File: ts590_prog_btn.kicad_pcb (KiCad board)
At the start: 2 copper layers, 18 parts, among them J1 DB9, SW1 PTT, SW2 PF2, SW3 PF4, SW4 PF1, SW5 PF3, SW6 UP, SW7 DOWN, SW8 MIC_EXT_PWR, SW9 PTT_LOCK

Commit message: added the first pcb draw
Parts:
- added REF**: EuroBoard_viertel_Type-I_80mmX50mm_holes, EuroBoard_Outline:EuroBoard_viertel_Type-I_80mmX50mm_holes, F.Cu at (109.5, 99.3)
- added REF**: Symbol_CreativeCommons_CopperTop_Type2_Small, Symbols:Symbol_CreativeCommons_CopperTop_Type2_Small, F.Cu at (176.5, 94.6)
- added REF**: Symbol_CreativeCommonsPublicDomain_CopperTop_Small, Symbols:Symbol_CreativeCommonsPublicDomain_CopperTop_Small, F.Cu at (149.2, 53.3)
- moved J1 95.2 mm to (173.7, 74.2), turned to 270 degrees
- moved SW9 60.7 mm to (125.0, 76.7), turned to 270 degrees
- moved SW8 59.8 mm to (161.8, 84.1), turned to 180 degrees
- moved SW3 52.8 mm to (163.1, 70.1)
- moved R2 49.5 mm to (164.3, 76.2)
- moved R6 46.3 mm to (149.4, 87.9), turned to 180 degrees
- moved SW7 40.1 mm to (152.9, 61.5)
- moved C1 39.2 mm to (164.3, 62.0)
- moved SW5 33.5 mm to (152.9, 70.1)
- moved R4 32.2 mm to (149.1, 76.2)
- moved R3 31.5 mm to (125.5, 61.5), turned to 90 degrees
- moved R5 31.2 mm to (149.4, 84.3)
- moved C2 26.7 mm to (138.2, 84.3), turned to 90 degrees
- moved SW6 22.9 mm to (142.7, 61.5)
- moved R1 22.7 mm to (121.9, 61.5), turned to 90 degrees
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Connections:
- J1 pad 6: Net-(J1-Pad6) -> (no net)
- J1 pad 9: Net-(J1-Pad9) -> (no net)
- SW8 pad 2: /EXTMIC -> (no net)
- SW8 pad 6: Net-(SW8-Pad6) -> (no net)
- SW9 pad 1: Net-(SW9-Pad1) -> (no net)
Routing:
- net /MICCN4_UP: track 0.00 -> 111.3 mm
- net /MICCN2_PTT: track 0.00 -> 80.3 mm
- net GNDA: track 0.00 -> 51.3 mm
- net /MICCN3_DOWN: track 0.00 -> 44.8 mm
- net /MIC_ELECT: track 0.00 -> 39.4 mm
- net Net-(R1-Pad1): track 0.00 -> 29.3 mm
- net /MICCN1_MIC: track 0.00 -> 27.6 mm
- net Net-(R3-Pad1): track 0.00 -> 15.1 mm
- net /MICCN5_8V: track 0.00 -> 14.2 mm
- net Net-(R4-Pad1): track 0.00 -> 14.2 mm
- net Net-(R2-Pad1): track 0.00 -> 11.2 mm
- net GND: track 0.00 -> 9.71 mm, vias 0 -> 1
- net Net-(C2-Pad1): track 0.00 -> 9.65 mm
- net /MICCN5_8V_PWRSW: track 0.00 -> 4.83 mm
- added copper zone on F.Cu, net GND
- added copper zone on B.Cu, net GNDA
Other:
- board outline added: 80 x 50 mm
- net class Default: trace_width 0.25 -> 0.254; via_dia 0.6 -> 1; via_drill 0.4 -> 0.5
- net class PWR added: clearance 0.2, trace_width 0.6, via_dia 1, via_drill 0.5
- board text added: "CT7AEZ"
- board text added: "Este trabalho está licenciado sob uma Licença Creative Commons Atribuição 4.0 Internacional. Para ver uma cópia desta licença, visite http://creativecommons.org/licenses/by/4.0/."

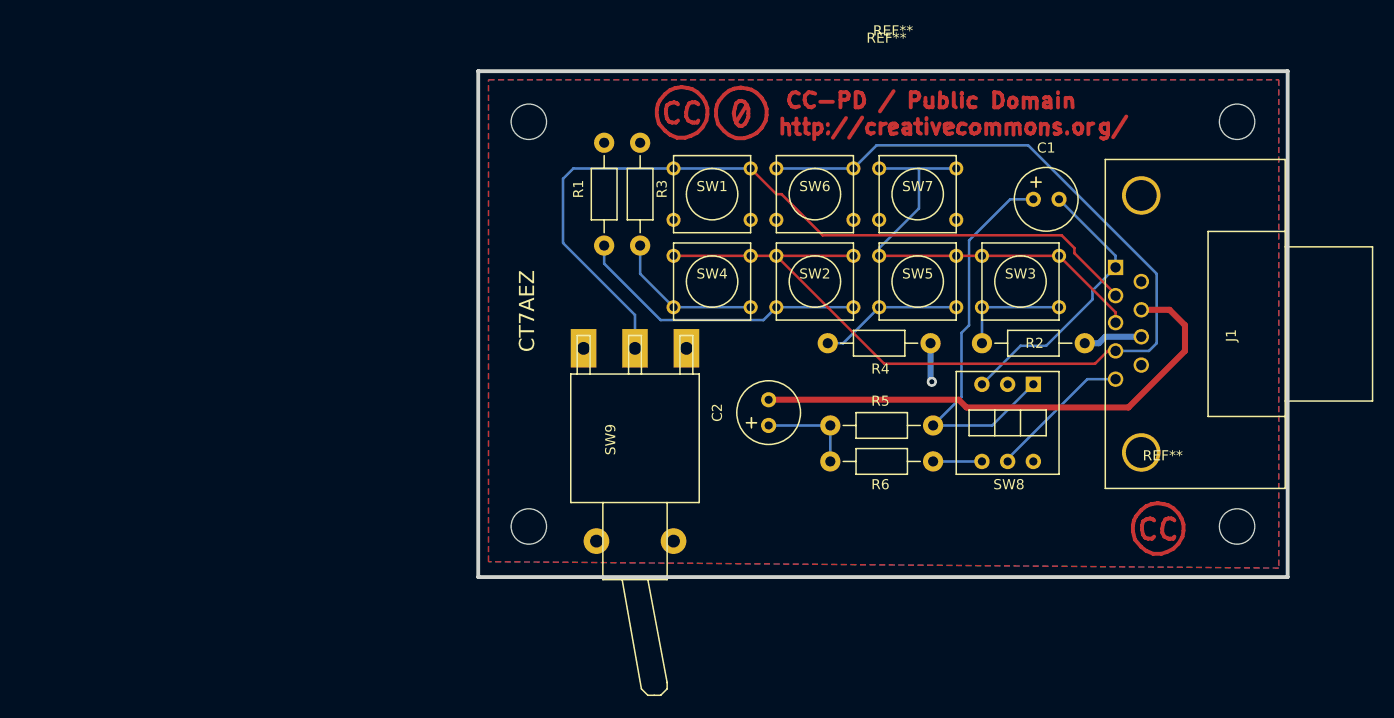
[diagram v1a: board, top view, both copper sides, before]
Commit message: add jack on pcb and new layout
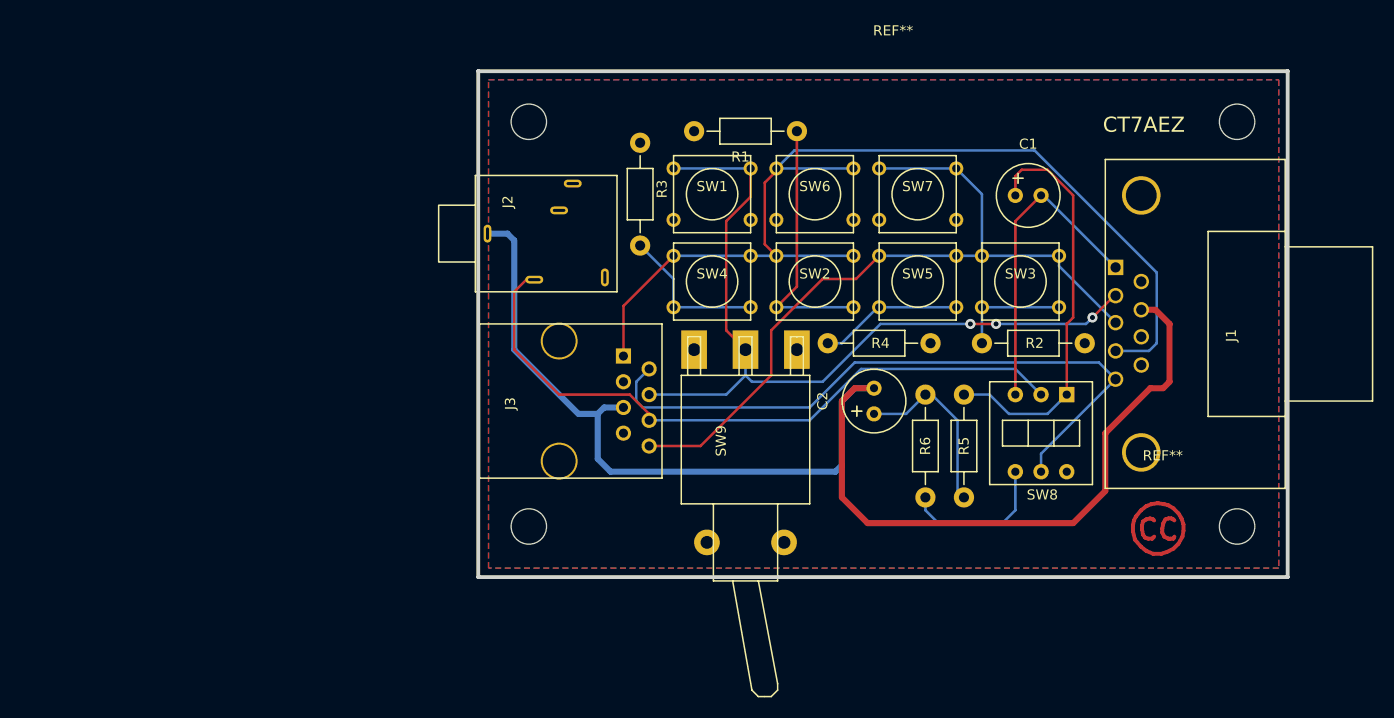
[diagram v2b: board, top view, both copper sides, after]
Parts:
- removed the REF** at (149.2, 53.3)
- added J2: JACK_TRS_6PINS, TS-590-Program-Function-extention:myaudiojack, F.Cu at (123.2, 71.1)
- added J3: RJ45, Connect:RJ45_8, F.Cu at (117.5, 81.9)
- moved R1 15.3 mm to (135.9, 55.2), turned to 180 degrees
- moved SW9 10.9 mm to (135.9, 76.8)
- moved C2 10.5 mm to (148.6, 83.2)
- moved R5 8.38 mm to (157.5, 86.4), turned to 90 degrees
- moved R6 4.58 mm to (153.7, 86.4), turned to 90 degrees
- moved SW8 3.45 mm to (165.1, 85.1)
- moved C1 1.82 mm to (162.6, 61.6)
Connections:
- SW8 pad 2: (no net) -> /EXTMIC
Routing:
- net GNDA: track 51.3 -> 131.7 mm
- net /EXTMIC: track 0.00 -> 67.3 mm
- net /MICCN5_8V: track 14.2 -> 66.1 mm
- net /MICCN3_DOWN: track 44.8 -> 77.1 mm
- net /MICCN5_8V_PWRSW: track 4.83 -> 15.0 mm
- net GND: track 9.71 -> 0.00 mm, vias 1 -> 0
- net /MICCN4_UP: track 111.3 -> 101.6 mm
- net Net-(C2-Pad1): track 9.65 -> 18.0 mm
- net /MICCN1_MIC: track 27.6 -> 31.0 mm
- net Net-(R1-Pad1): track 29.3 -> 26.5 mm
- net /MIC_ELECT: track 39.4 -> 40.6 mm
- net /MICCN2_PTT: track 80.3 -> 80.5 mm, vias 0 -> 3
- added copper zone on B.Cu, net GND
- removed copper zone on B.Cu, net GNDA
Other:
- board text removed: "Este trabalho está licenciado sob uma Licença Creative Commons Atribuição 4.0 Internacional. Para ver uma cópia desta licença, visite http://creativecommons.org/licenses/by/4.0/."

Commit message: Corrected the mic pwr selection on pcb and sch.
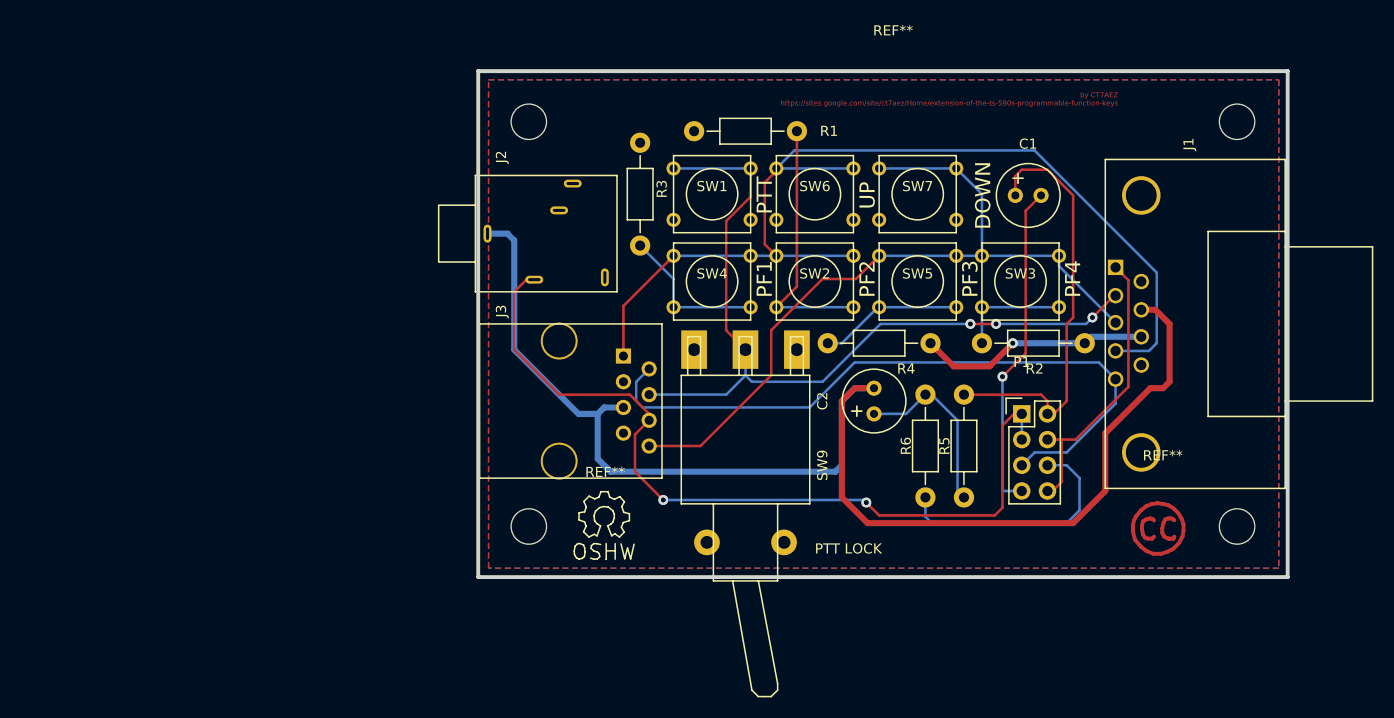
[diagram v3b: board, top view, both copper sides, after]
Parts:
- removed SW8: MIC_EXT_PWR, Discret:swdip3
- added P1: CONN_02X04, Pin_Headers:Pin_Header_Straight_2x04, F.Cu at (163.2, 83.2)
- added REF**: Symbol_OSHW-Logo_SilkScreen, Symbols:Symbol_OSHW-Logo_SilkScreen, F.Cu at (121.9, 93.3)
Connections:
- C1 pad 2: /MICCN1_MIC -> Net-(C1-Pad2)
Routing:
- net Net-(C1-Pad2): track 0.00 -> 32.9 mm, vias 0 -> 1
- net GND: track 0.00 -> 23.0 mm, vias 0 -> 1
- net /EXTMIC: track 67.3 -> 82.6 mm, vias 0 -> 2
- net /MICCN5_8V_PWRSW: track 15.0 -> 24.8 mm
- net /MICCN1_MIC: track 31.0 -> 28.5 mm
- net /MICCN5_8V: track 66.1 -> 68.1 mm
- net /MIC_ELECT: track 40.6 -> 41.7 mm
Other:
- board text added: "DOWN"
- board text added: "MIC PWR"
- board text added: "NO MIC PWR"
- board text added: "PF1"
- board text added: "PF2"
- board text added: "PF3"
- board text added: "PF4"
- board text added: "PTT"
- board text added: "PTT LOCK"
- board text added: "UP"
- board text added: "by CT7AEZ https://sites.google.com/site/ct7aez/Home/extension-of-the-ts-590s-programmable-function-keys"
- board text removed: "CT7AEZ"

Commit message: small changes on pcb
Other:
- rule pad_to_mask_clearance: 0 -> 0.2
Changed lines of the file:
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@@
     (pad_size 1.5 1.5)
     (pad_drill 0.6)
-    (pad_to_mask_clearance 0)
+    (pad_to_mask_clearance 0.2)
     (aux_axis_origin 0 0)
     (visible_elements FFFFFF7F)
     (pcbplotparams
-      (layerselection 0x00030_80000001)
-      (usegerberextensions false)
+      (layerselection 0x030f0_80000001)
+      (usegerberextensions true)
       (excludeedgelayer true)
       (linewidth 0.100000)
@@
       (outputformat 1)
       (mirror false)
-      (drillshape 1)
+      (drillshape 0)
       (scaleselection 1)
-      (outputdirectory ""))
+      (outputdirectory gerb/))
   )
   (net 0 "")
@@
     (add_net GNDA)
   )
+  (module Capacitors_Elko_ThroughHole:Elko_vert_11.2x6.3mm_RM2.5 (layer F.Cu)
+    (at 148.59 83.185 90)
+    (descr "Electrolytic Capacitor, vertical, diameter 6,3mm, RM 2,5mm, radial,")
+    (tags "Electrolytic Capacitor, vertical, diameter 6,3mm, RM 2,5mm, Elko, Electrolytkondensator, Kondensator gepolt, Durchmesser 6,3mm, radial,")
+    (fp_text reference C2 (at 1.27 -5.08 90) (layer F.SilkS)
+      (effects (font (size 1 1) (thickness 0.15)))
+    )
+    (fp_text value 10u (at 1.27 5.08 90) (layer F.Fab)
+      (effects (font (size 1 1) (thickness 0.15)))
+    )
+    (fp_line (start 0.26924 -2.19964) (end 0.26924 -1.19888) (layer F.SilkS) (width 0.15))
+    (fp_line (start -0.23114 -1.69926) (end 0.76962 -1.69926) (layer F.SilkS) (width 0.15))
+    (fp_circle (center 1.27 0) (end 4.4196 0) (layer F.SilkS) (width 0.15))
+    (pad 2 thru_hole circle (at 2.54 0 90) (size 1.50114 1.50114) (drill 0.8001) (layers *.Cu *.Mask F.SilkS)
+      (net 3 GNDA))
+    (pad 1 thru_hole circle (at 0 0 90) (size 1.50114 1.50114) (drill 0.8001) (layers *.Cu *.Mask F.SilkS)
+      (net 4 "Net-(C2-Pad1)"))
+    (model Capacitors_Elko_ThroughHole.3dshapes/Elko_vert_11.2x6.3mm_RM2.5.wrl
+      (at (xyz 0 0 0))
+      (scale (xyz 1 1 1))
+      (rotate (xyz 0 0 0))
+    )
+  )
   (module EuroBoard_Outline:EuroBoard_viertel_Type-I_80mmX50mm_holes (layer F.Cu)
     (at 109.474 99.314)
     (descr "Outline, Eurocard 1/4, Type I,  80x50mm, with holes 3,5mm,")
     (tags "Outline, Eurocard 1/4, Type I, 80x50mm, with holes 3,5mm,")
-    (fp_text reference REF** (at 41.00068 -54.0004) (layer F.SilkS)
+    (fp_text reference REF** (at 41.00068 -54.0004) (layer F.SilkS) hide
       (effects (font (size 1 1) (thickness 0.15)))
     )
@@
     (pad 1 thru_hole circle (at 0 0) (size 1.50114 1.50114) (drill 0.8001) (layers *.Cu *.Mask F.SilkS)
       (net 2 /MIC_ELECT))
-    (model Capacitors_Elko_ThroughHole.3dshapes/Elko_vert_11.2x6.3mm_RM2.5.wrl
-      (at (xyz 0 0 0))
-      (scale (xyz 1 1 1))
-      (rotate (xyz 0 0 0))
-    )
-  )
-  (module Capacitors_Elko_ThroughHole:Elko_vert_11.2x6.3mm_RM2.5 (layer F.Cu)
-    (at 148.59 83.185 90)
-    (descr "Electrolytic Capacitor, vertical, diameter 6,3mm, RM 2,5mm, radial,")
-    (tags "Electrolytic Capacitor, vertical, diameter 6,3mm, RM 2,5mm, Elko, Electrolytkondensator, Kondensator gepolt, Durchmesser 6,3mm, radial,")
-    (fp_text reference C2 (at 1.27 -5.08 90) (layer F.SilkS)
-      (effects (font (size 1 1) (thickness 0.15)))
-    )
-    (fp_text value 10u (at 1.27 5.08 90) (layer F.Fab)
-      (effects (font (size 1 1) (thickness 0.15)))
-    )
-    (fp_line (start 0.26924 -2.19964) (end 0.26924 -1.19888) (layer F.SilkS) (width 0.15))
-    (fp_line (start -0.23114 -1.69926) (end 0.76962 -1.69926) (layer F.SilkS) (width 0.15))
-    (fp_line (start 0.26924 -1.69926) (end 0.76962 -1.69926) (layer F.Cu) (width 0.15))
-    (fp_line (start 0.26924 -1.69926) (end 0.26924 -2.19964) (layer F.Cu) (width 0.15))
-    (fp_line (start -0.23114 -1.69926) (end 0.26924 -1.69926) (layer F.Cu) (width 0.15))
-    (fp_line (start 0.26924 -1.69926) (end 0.26924 -1.30048) (layer F.Cu) (width 0.15))
-    (fp_line (start 0.26924 -1.30048) (end 0.26924 -1.19888) (layer F.Cu) (width 0.15))
-    (fp_circle (center 1.27 0) (end 4.4196 0) (layer F.SilkS) (width 0.15))
-    (pad 2 thru_hole circle (at 2.54 0 90) (size 1.50114 1.50114) (drill 0.8001) (layers *.Cu *.Mask F.SilkS)
-      (net 3 GNDA))
-    (pad 1 thru_hole circle (at 0 0 90) (size 1.50114 1.50114) (drill 0.8001) (layers *.Cu *.Mask F.SilkS)
-      (net 4 "Net-(C2-Pad1)"))
     (model Capacitors_Elko_ThroughHole.3dshapes/Elko_vert_11.2x6.3mm_RM2.5.wrl
       (at (xyz 0 0 0))
@@
     (descr "Symbol, Creative Commons, CopperTop, Type 2, Small,")
     (tags "Symbol, Creative Commons, CopperTop, Type 2, Small,")
-    (fp_text reference REF** (at 0.59944 -7.29996) (layer F.SilkS)
+    (fp_text reference REF** (at 0.59944 -7.29996) (layer F.SilkS) hide
       (effects (font (size 1 1) (thickness 0.15)))
     )
@@
     (descr "Symbol, OSHW-Logo, Silk Screen,")
     (tags "Symbol, OSHW-Logo, Silk Screen,")
-    (fp_text reference REF** (at 0.09906 -4.38912) (layer F.SilkS)
-      (effects (font (size 1 1) (thickness 0.15)))
-    )
+    (fp_text reference REF** (at 0.09906 -4.38912) (layer F.SilkS) hide
+      (effects (font (size 1 1) (thickness 0.15)))
+    )
